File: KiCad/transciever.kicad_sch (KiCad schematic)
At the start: 5 parts, among them J5 DE9_Pins_MountingHoles, U4 MCP2551-I-SN

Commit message: modificacions cadlab
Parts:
- removed C_out3: 100nF, Capacitor_SMD:C_0805_2012Metric_Pad1.18x1.45mm_HandSolder, symbol Device:C
- removed J5: DE9_Pins_MountingHoles, Connector_Dsub:DSUB-9_Pins_Horizontal_P2.77x2.84mm_EdgePinOffset4.94mm_Housed_MountingHolesOffset4.94mm, symbol Connector:DE9_Pins_MountingHoles
- removed R13: 12O, Resistor_SMD:R_0805_2012Metric_Pad1.20x1.40mm_HandSolder, symbol Device:R
- removed R14: 10k, Resistor_SMD:R_0805_2012Metric_Pad1.20x1.40mm_HandSolder, symbol Device:R
- removed U4: MCP2551-I-SN, Package_SO:SOIC-8_3.9x4.9mm_P1.27mm, symbol Interface_CAN_LIN:MCP2551-I-SN
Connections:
- no-connect marks 7 -> 0
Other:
- note removed: "Pull up a prop del XIP"
- note removed: "TRANSCIEVER"

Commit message: he canviat el micro
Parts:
- added C_out3: 100nF, symbol Device:C
- added J2: Conn_01x03, symbol Connector_Generic:Conn_01x03
- added R13: 12O, symbol Device:R
- added U4: MCP2551-I-SN, Package_SO:SOIC-8_3.9x4.9mm_P1.27mm, symbol Interface_CAN_LIN:MCP2551-I-SN
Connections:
- new net: C_out3.2, U4.3 (VDD)
- new net BUS_CANH: J2.1 (Pin_1), R13.1, U4.7 (CANH)
- new net BUS_CANL: J2.2 (Pin_2), R13.2, U4.6 (CANL)
- new net CANRX: U4.4 (RXD)
- new net CANTX: U4.1 (TXD)
- new net GND: C_out3.1, J2.3 (Pin_3), U4.2 (VSS), U4.8 (Rs)
- no-connect marks 0 -> 1
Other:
- note added: "Pull up a prop del XIP"
- note added: "TRANSCIEVER"

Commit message: ERC i footprints
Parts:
- C_out3: footprint (none) -> Capacitor_SMD:C_0805_2012Metric_Pad1.18x1.45mm_HandSolder
- J2: footprint (none) -> Connector_PinHeader_2.54mm:PinHeader_1x03_P2.54mm_Vertical
- R13: footprint (none) -> Resistor_SMD:R_0805_2012Metric_Pad1.20x1.40mm_HandSolder
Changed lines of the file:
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@@
 			)
 		)
-		(property "Footprint" ""
+		(property "Footprint" "Connector_PinHeader_2.54mm:PinHeader_1x03_P2.54mm_Vertical"
 			(at 175.26 101.6 0)
 			(effects
@@
 			)
 		)
-		(property "Footprint" ""
+		(property "Footprint" "Resistor_SMD:R_0805_2012Metric_Pad1.20x1.40mm_HandSolder"
 			(at 153.162 100.33 90)
 			(effects
@@
 		(dnp no)
 		(fields_autoplaced yes)
-		(property "Reference" "#PWR016"
+		(property "Reference" "#PWR0103"
 			(at 167.64 111.76 0)
 			(effects
@@
 			(project "PROJECTE_LLUMS"
 				(path "/b4874c87-978f-427f-bc45-3635f8629977/cd13a3ea-30b8-4fef-9eee-500876d417cb"
-					(reference "#PWR016")
+					(reference "#PWR0103")
 					(unit 1)
 				)
@@
 			)
 		)
-		(property "Footprint" ""
+		(property "Footprint" "Capacitor_SMD:C_0805_2012Metric_Pad1.18x1.45mm_HandSolder"
 			(at 138.1252 88.9 0)
 			(effects

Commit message: routing
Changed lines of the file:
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@@
+		)
+	)
+	(label "VDD"
+		(at 133.35 78.74 0)
+		(effects
+			(font
+				(size 1.27 1.27)
+			)
+			(justify left bottom)
 		)
 	)
@@
 		)
 		(property "Value" "MCP2551-I-SN"
-			(at 139.192 90.678 0)
-			(effects
-				(font
+			(at 138.176 109.982 0)
+			(effects
+				(font

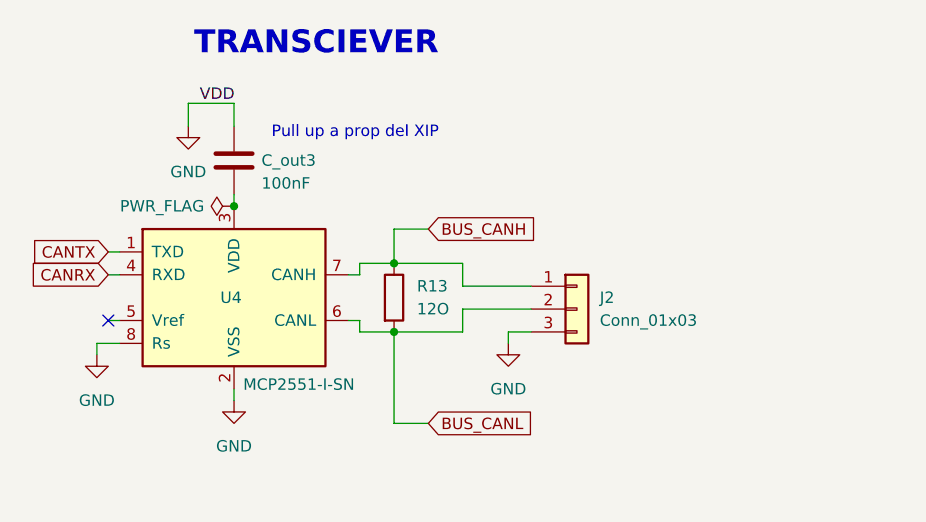
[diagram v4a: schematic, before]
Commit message: alguns errors de CADLAB i he canivat d'ordre els LEDs i els drivers a la PCB.
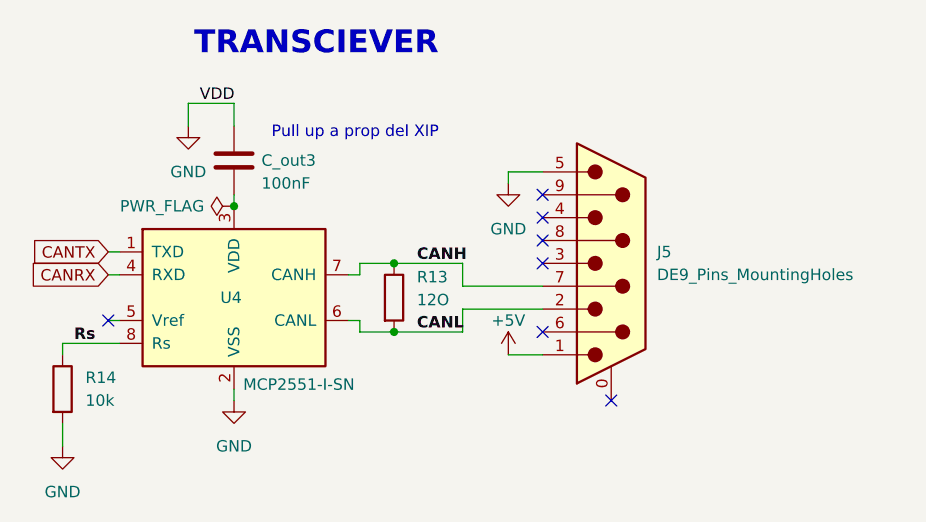
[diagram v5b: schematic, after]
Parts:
- removed J2: Conn_01x03, Connector_PinHeader_2.54mm:PinHeader_1x03_P2.54mm_Vertical, symbol Connector_Generic:Conn_01x03
- added J5: DE9_Pins_MountingHoles, Connector_Dsub:DSUB-9_Pins_Horizontal_P2.77x2.84mm_EdgePinOffset4.94mm_Housed_MountingHolesOffset4.94mm, symbol Connector:DE9_Pins_MountingHoles
- added R14: 10k, Resistor_SMD:R_0805_2012Metric_Pad1.20x1.40mm_HandSolder, symbol Device:R
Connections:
- net GND: now also J5.5, R14.2; no longer U4.8 (Rs)
- net BUS_CANH renamed CANH
- net CANH: now also J5.7
- net BUS_CANL renamed CANL
- net CANL: now also J5.2
- new net +5V: J5.1
- new net Rs: R14.1, U4.8 (Rs)
- no-connect marks 1 -> 7
